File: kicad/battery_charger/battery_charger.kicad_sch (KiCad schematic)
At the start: 19 parts, among them J1 Conn_01x03_Pin, J2 USB_B_Micro, Q1 Q_PMOS_DSG, U1 TPS61200DRC, U2 MCP73831-2-OT

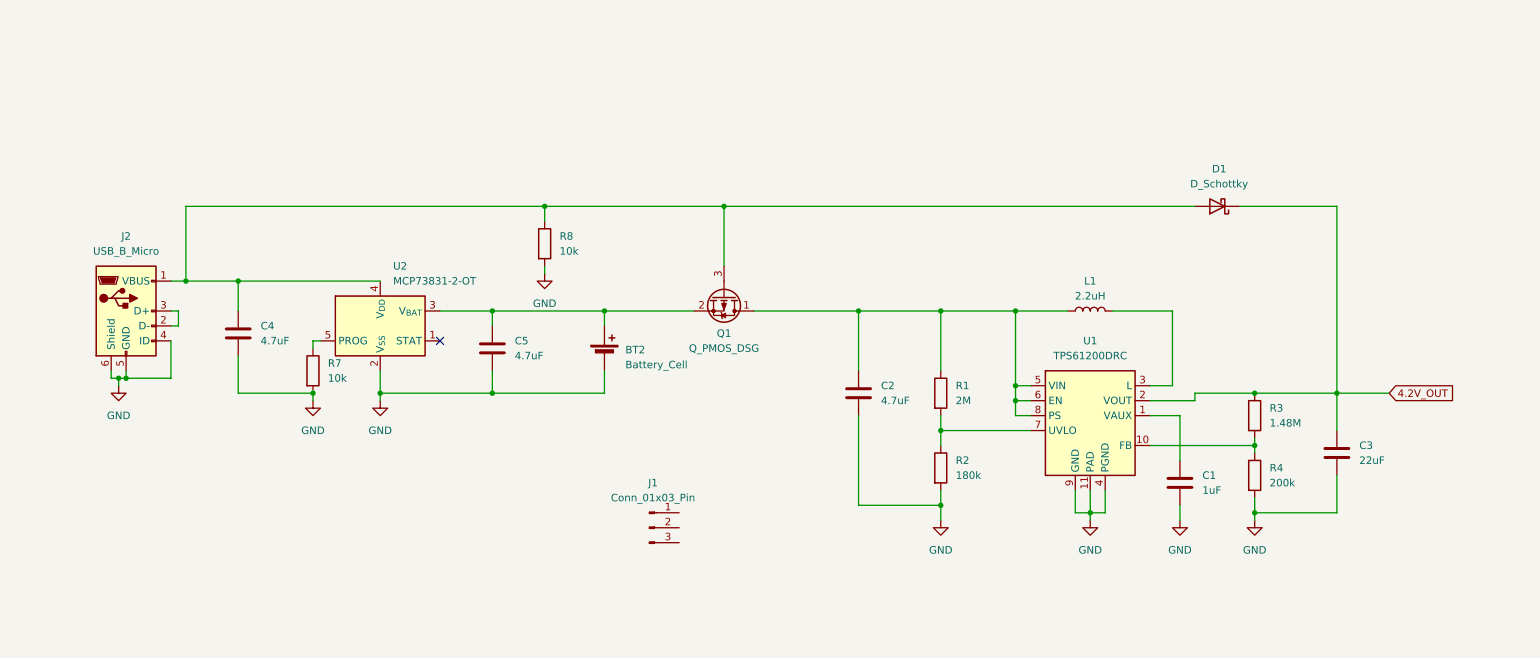
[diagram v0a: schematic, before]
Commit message: USB C compatible, added battery level indicator button
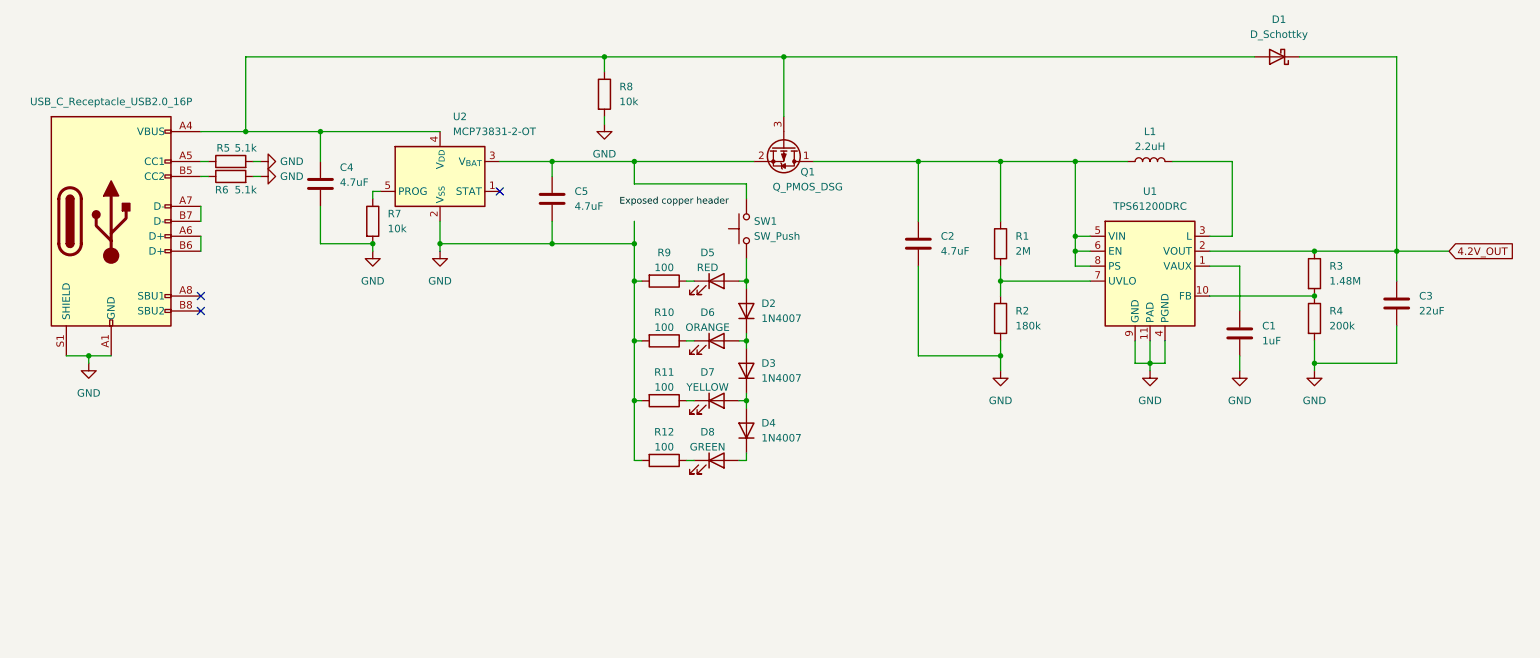
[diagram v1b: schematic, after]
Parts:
- removed BT2: Battery_Cell, symbol Device:Battery_Cell
- removed J1: Conn_01x03_Pin, symbol Connector:Conn_01x03_Pin
- removed J2: USB_B_Micro, symbol Connector:USB_B_Micro
- added D2, D3, D4: 1N4007, Diode_THT:D_DO-41_SOD81_P10.16mm_Horizontal, symbol Diode:1N4007
- added D5: RED, symbol Device:LED
- added D6: ORANGE, symbol Device:LED
- added D7: YELLOW, symbol Device:LED
- added D8: GREEN, symbol Device:LED
- added J1: USB_C_Receptacle_USB2.0_16P, symbol Connector:USB_C_Receptacle_USB2.0_16P
- added R10, R11, R12, R9: 100, symbol Device:R
- added R5, R6: 5.1k, symbol Device:R
- added SW1: SW_Push, symbol Switch:SW_Push
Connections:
- net GND: now also J1.A1 (GND), J1.A12 (GND), J1.B1 (GND), J1.B12 (GND), J1.S1 (SHIELD), R10.2, R11.2, R12.2, R5.2, R6.2, R9.2
- net at C5.1, Q1.2 (S), U2.3 (V_{BAT}): now also SW1.2
- net at C4.1, D1.2 (A), Q1.3 (G)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: now also J1.A4 (VBUS), J1.A9 (VBUS), J1.B4 (VBUS), J1.B9 (VBUS)
- new net: D5.1 (K), R9.1
- new net: D2.2 (A), D5.2 (A), SW1.1
- new net: D2.1 (K), D3.2 (A), D6.2 (A)
- new net: D4.1 (K), D8.2 (A)
- new net: D3.1 (K), D4.2 (A), D7.2 (A)
- new net: D8.1 (K), R12.1
- new net: J1.A5 (CC1), R5.1
- new net: J1.A6 (D+), J1.B6 (D+)
- new net: J1.A7 (D-), J1.B7 (D-)
- new net: J1.B5 (CC2), R6.1
- new net: D7.1 (K), R11.1
- new net: D6.1 (K), R10.1
- no-connect marks 1 -> 3
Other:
- title: (none) -> USB C Battery Charger and Source
- moved on the sheet: C1, C2, C3, C4, C5, D1, L1, Q1, R1, R2, R3, R4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

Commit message: made the pcb
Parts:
- C1: footprint (none) -> Capacitor_SMD:C_0402_1005Metric
- C2, C4, C5: footprint (none) -> Capacitor_SMD:C_0603_1608Metric
- C3: footprint (none) -> Capacitor_SMD:C_0805_2012Metric
- D1: footprint (none) -> Diode_SMD:D_0603_1608Metric
- D5, D6, D7, D8: footprint (none) -> LED_SMD:LED_0201_0603Metric
- J1: footprint (none) -> Connector_USB:USB_C_Receptacle_Amphenol_12401548E4-2A
- L1: footprint (none) -> Inductor_SMD:L_0603_1608Metric
- Q1: footprint (none) -> Package_DirectFET:DirectFET_MX
- R1, R10, R11, R12, R2, R3, R4, R5, R6, R7, R8, R9: footprint (none) -> Resistor_SMD:R_0603_1608Metric
- SW1: footprint (none) -> Button_Switch_THT:SW_PUSH_6mm
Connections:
- net at J1.A6 (D+): no longer J1.B6 (D+)
- net at J1.A7 (D-): no longer J1.B7 (D-)
- no-connect marks 3 -> 7
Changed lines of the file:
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@@
 	)
 	(no_connect
+		(at 52.07 62.23)
+	)
+	(no_connect
+		(at 52.07 69.85)
+	)
+	(no_connect
 		(at 52.07 77.47)
 	)
@@
 	)
 	(no_connect
+		(at 52.07 67.31)
+	)
+	(no_connect
+		(at 52.07 64.77)
+	)
+	(no_connect
 		(at 102.87 59.69)
 	)
@@
 	(wire
 		(pts
-			(xy 52.07 67.31) (xy 52.07 69.85)
-		)
-		(stroke
-			(width 0)
-			(type default)
-		)
-	)
-	(wire
-		(pts
 			(xy 241.3 69.85) (xy 255.27 69.85)
 		)
@@
 	(wire
 		(pts
-			(xy 52.07 62.23) (xy 52.07 64.77)
-		)
-		(stroke
-			(width 0)
-			(type default)
-		)
-	)
-	(wire
-		(pts
 			(xy 92.71 64.77) (xy 92.71 68.58)
 		)
@@
 			)
 		)
-		(property "Footprint" ""
+		(property "Footprint" "Package_DirectFET:DirectFET_MX"
 			(at 153.67 57.15 0)
 			(effects
@@
 			)
 		)
-		(property "Footprint" ""
+		(property "Footprint" "Resistor_SMD:R_0603_1608Metric"
 			(at 130.81 73.152 90)
 			(effects
@@
 			)
 		)
-		(property "Footprint" ""
+		(property "Footprint" "Button_Switch_THT:SW_PUSH_6mm"
 			(at 139.7 66.04 0)
 			(effects
@@
 			)
 		)
-		(property "Footprint" ""
+		(property "Footprint" "Resistor_SMD:R_0603_1608Metric"
 			(at 79.502 64.77 90)
 			(effects
@@
 			)
 		)
-		(property "Footprint" ""
+		(property "Footprint" "Resistor_SMD:R_0603_1608Metric"
 			(at 130.81 103.632 90)
 			(effects
@@
 			)
 		)
-		(property "Footprint" ""
+		(property "Footprint" "Capacitor_SMD:C_0402_1005Metric"
 			(at 229.5652 87.63 0)
 			(effects
@@
 			)
 		)
-		(property "Footprint" ""
+		(property "Footprint" "Connector_USB:USB_C_Receptacle_Amphenol_12401548E4-2A"
 			(at 40.64 64.77 0)
 			(effects
@@
 			)
 		)
-		(property "Footprint" ""
+		(property "Footprint" "Capacitor_SMD:C_0603_1608Metric"
 			(at 73.3552 62.23 0)
 			(effects
@@
 			)
 		)
-		(property "Footprint" ""
+		(property "Footprint" "Resistor_SMD:R_0603_1608Metric"
 			(at 130.81 93.472 90)
 			(effects
@@
 			)
 		)
-		(property "Footprint" ""
+		(property "Footprint" "Resistor_SMD:R_0603_1608Metric"
 			(at 239.522 73.66 90)
 			(effects
@@
 			)
 		)
-		(property "Footprint" ""
+		(property "Footprint" "Resistor_SMD:R_0603_1608Metric"
 			(at 57.15 58.928 90)
 			(effects
@@
 			)
 		)
-		(property "Footprint" ""
+		(property "Footprint" "Resistor_SMD:R_0603_1608Metric"
 			(at 57.15 56.388 90)
 			(effects
@@
 			)
 		)
-		(property "Footprint" ""
+		(property "Footprint" "LED_SMD:LED_0201_0603Metric"
 			(at 139.7 95.25 0)
 			(effects
@@
 			)
 		)
-		(property "Footprint" ""
+		(property "Footprint" "LED_SMD:LED_0201_0603Metric"
 			(at 139.7 74.93 0)
 			(effects
@@
 			)
 		)
-		(property "Footprint" ""
+		(property "Footprint" "LED_SMD:LED_0201_0603Metric"
 			(at 139.7 105.41 0)
 			(effects
@@
 			)
 		)
-		(property "Footprint" ""
+		(property "Footprint" "Diode_SMD:D_0603_1608Metric"
 			(at 234.95 36.83 0)
 			(effects
@@
 			)
 		)
-		(property "Footprint" ""
+		(property "Footprint" "Inductor_SMD:L_0603_1608Metric"
 			(at 213.36 54.61 0)
 			(effects
@@
 			)
 		)
-		(property "Footprint" ""
+		(property "Footprint" "LED_SMD:LED_0201_0603Metric"
 			(at 139.7 85.09 0)
 			(effects
@@
 			)
 		)
-		(property "Footprint" ""
+		(property "Footprint" "Resistor_SMD:R_0603_1608Metric"
 			(at 186.182 81.28 90)
 			(effects
@@
 			)
 		)
-		(property "Footprint" ""
+		(property "Footprint" "Resistor_SMD:R_0603_1608Metric"
 			(at 130.81 83.312 90)
 			(effects
@@
 			)
 		)
-		(property "Footprint" ""
+		(property "Footprint" "Resistor_SMD:R_0603_1608Metric"
 			(at 118.872 43.18 90)
 			(effects
@@
 			)
 		)
-		(property "Footprint" ""
+		(property "Footprint" "Capacitor_SMD:C_0603_1608Metric"
 			(at 174.9552 72.39 0)
 			(effects
@@
 			)
 		)
-		(property "Footprint" ""
+		(property "Footprint" "Resistor_SMD:R_0603_1608Metric"
 			(at 186.182 68.58 90)
 			(effects
@@
 			)
 		)
-		(property "Footprint" ""
+		(property "Footprint" "Capacitor_SMD:C_0805_2012Metric"
 			(at 256.2352 82.55 0)
 			(effects
@@
 			)
 		)
-		(property "Footprint" ""
+		(property "Footprint" "Resistor_SMD:R_0603_1608Metric"
 			(at 239.522 81.28 90)
 			(effects
@@
 			)
 		)
-		(property "Footprint" ""
+		(property "Footprint" "Capacitor_SMD:C_0603_1608Metric"
 			(at 112.7252 64.77 0)
 			(effects

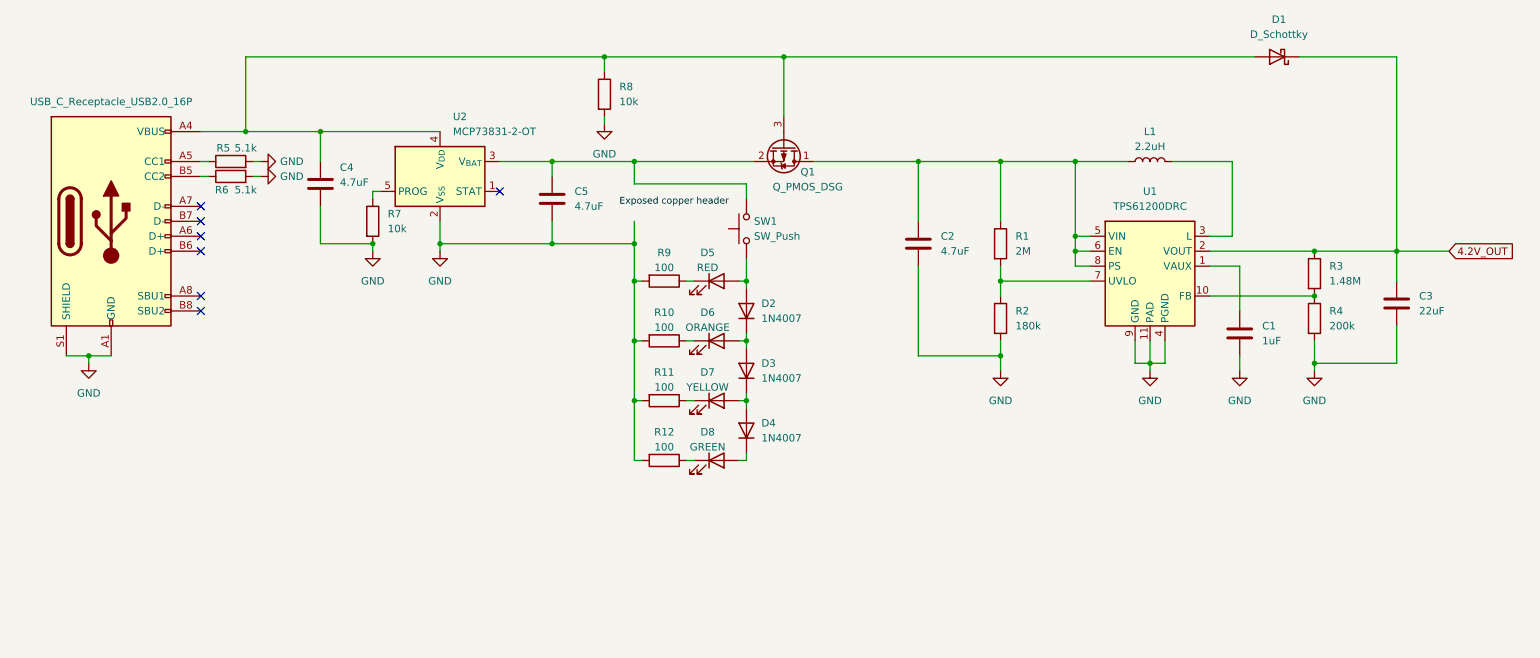
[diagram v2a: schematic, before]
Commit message: changed to usb b micro, made design longer and thinner
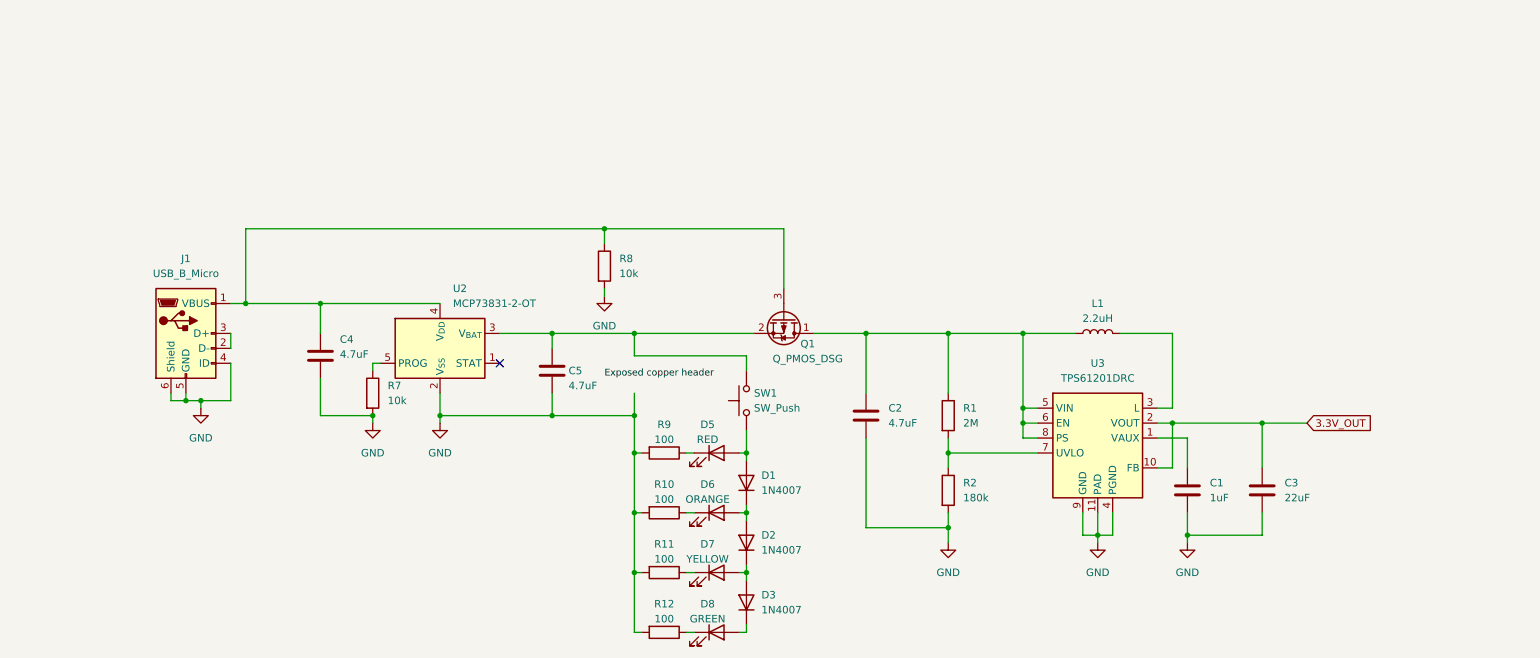
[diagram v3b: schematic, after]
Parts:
- removed D1: D_Schottky, Diode_SMD:D_0603_1608Metric, symbol Device:D_Schottky
- removed D4: 1N4007, Diode_THT:D_DO-41_SOD81_P10.16mm_Horizontal, symbol Diode:1N4007
- removed J1: USB_C_Receptacle_USB2.0_16P, Connector_USB:USB_C_Receptacle_Amphenol_12401548E4-2A, symbol Connector:USB_C_Receptacle_USB2.0_16P
- removed R3: 1.48M, Resistor_SMD:R_0603_1608Metric, symbol Device:R
- removed R4: 200k, Resistor_SMD:R_0603_1608Metric, symbol Device:R
- removed R5, R6: 5.1k, Resistor_SMD:R_0603_1608Metric, symbol Device:R
- removed U1: TPS61200DRC, Package_SON:Texas_S-PVSON-N10_ThermalVias, symbol Regulator_Switching:TPS61200DRC
- added D1: 1N4007, Library:SODFL3818X130N, symbol Diode:1N4007
- added J1: USB_B_Micro, Connector_USB:USB_Micro-B_Amphenol_10118193-0001LF_Horizontal, symbol Connector:USB_B_Micro
- added U3: TPS61201DRC, Library:TPS61201DRC, symbol Regulator_Switching:TPS61201DRC
- D2, D3: footprint Diode_THT:D_DO-41_SOD81_P10.16mm_Horizontal -> Library:SODFL3818X130N
- SW1: footprint Button_Switch_THT:SW_PUSH_6mm -> Button_Switch_SMD:SW_Push_1P1T-MP_NO_Horizontal_Alps_SKRTLAE010
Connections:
- net GND: now also J1.4 (ID), J1.5 (GND), J1.6 (Shield), U3.11 (PAD), U3.4 (PGND), U3.9 (GND)
- net at C2.1, L1.1, Q1.1 (D)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: now also U3.5 (VIN), U3.6 (EN), U3.8 (PS)
- net at C4.1, Q1.3 (G), R8.1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: now also J1.1 (VBUS)
- net at D5.2 (A), SW1.1: now also D1.2 (A); no longer D2.2 (A)
- net at D2.1 (K), D3.2 (A): now also D7.2 (A); no longer D6.2 (A)
- net at D8.2 (A): now also D3.1 (K)
- net at C1.1: now also U3.1 (VAUX)
- net at L1.2: now also U3.3 (L)
- net at R1.2, R2.1: now also U3.7 (UVLO)
- net 4.2V_OUT renamed 3.3V_OUT
- net 3.3V_OUT: now also U3.10 (FB), U3.2 (VOUT)
- new net: D1.1 (K), D2.2 (A), D6.2 (A)
- new net: J1.2 (D-), J1.3 (D+)
- no-connect marks 7 -> 1
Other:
- moved on the sheet: C1, C2, C3, C4, C5, D5, D6, D7, D8, L1, Q1, R1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

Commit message: neues aus dem labor
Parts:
- removed Q1: Q_PMOS_DSG, Package_DirectFET:DirectFET_MX, symbol Device:Q_PMOS_DSG
- added Q1: Q_PMOS_GSD, Package_TO_SOT_SMD:SOT-23-3, symbol Device:Q_PMOS_GSD
- D1, D2, D3: footprint Library:SODFL3818X130N -> Diode_SMD:D_SOD-123F
- D5, D6, D7, D8: footprint LED_SMD:LED_0201_0603Metric -> LED_SMD:LED_0402_1005Metric
- SW1: footprint Button_Switch_SMD:SW_Push_1P1T-MP_NO_Horizontal_Alps_SKRTLAE010 -> Button_Switch_SMD:SW_SPST_B3U-1000P
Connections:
- net at C2.1, L1.1, R1.1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: now also Q1.3 (D)
- net at C5.1, SW1.2, U2.3 (V_{BAT}): now also Q1.2 (S)
- net at C4.1, J1.1 (VBUS), R8.1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: now also Q1.1 (G)
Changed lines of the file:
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@@
-	)
-	(symbol
-		(lib_id "Device:Q_PMOS_DSG")
-		(at 151.13 81.28 270)
-		(unit 1)
-		(exclude_from_sim no)
-		(in_bom yes)
-		(on_board yes)
-		(dnp no)
-		(property "Reference" "Q1"
-			(at 155.194 85.598 90)
-			(effects
-				(font
-					(size 1.27 1.27)
-				)
-			)
-		)
-		(property "Value" "Q_PMOS_DSG"
-			(at 155.194 88.138 90)
-			(effects
-				(font
-					(size 1.27 1.27)
-				)
-			)
-		)
-		(property "Footprint" "Package_DirectFET:DirectFET_MX"
-			(at 153.67 86.36 0)
-			(effects
-				(font
-					(size 1.27 1.27)
-				)
-				(hide yes)
-			)
-		)
-		(property "Datasheet" "~"
-			(at 151.13 81.28 0)
-			(effects
-				(font
-					(size 1.27 1.27)
-				)
-				(hide yes)
-			)
-		)
-		(property "Description" "P-MOSFET transistor, drain/source/gate"
-			(at 151.13 81.28 0)
-			(effects
-				(font
-					(size 1.27 1.27)
-				)
-				(hide yes)
-			)
-		)
-		(pin "2"
-		)
-		(pin "1"
-		)
-		(pin "3"
-		)
-		(instances
-			(project ""
-				(path "/add37744-b832-4f24-98d5-20347e778715"
-					(reference "Q1")
-					(unit 1)
-				)
-			)
-		)
 	)
 	(symbol
@@
 			)
 		)
-		(property "Footprint" "Button_Switch_SMD:SW_Push_1P1T-MP_NO_Horizontal_Alps_SKRTLAE010"
+		(property "Footprint" "Button_Switch_SMD:SW_SPST_B3U-1000P"
 			(at 139.7 95.25 0)
 			(effects
@@
 	)
 	(symbol
+		(lib_id "Device:Q_PMOS_GSD")
+		(at 151.13 81.28 270)
+		(unit 1)
+		(exclude_from_sim no)
+		(in_bom yes)
+		(on_board yes)
+		(dnp no)
+		(property "Reference" "Q1"
+			(at 151.13 87.63 90)
+			(effects
+				(font
+					(size 1.27 1.27)
+				)
+			)
+		)
+		(property "Value" "Q_PMOS_GSD"
+			(at 156.718 90.17 90)
+			(effects
+				(font
+					(size 1.27 1.27)
+				)
+			)
+		)
+		(property "Footprint" "Package_TO_SOT_SMD:SOT-23-3"
+			(at 153.67 86.36 0)
+			(effects
+				(font
+					(size 1.27 1.27)
+				)
+				(hide yes)
+			)
+		)
+		(property "Datasheet" "~"
+			(at 151.13 81.28 0)
+			(effects
+				(font
+					(size 1.27 1.27)
+				)
+				(hide yes)
+			)
+		)
+		(property "Description" "P-MOSFET transistor, gate/source/drain"
+			(at 151.13 81.28 0)
+			(effects
+				(font
+					(size 1.27 1.27)
+				)
+				(hide yes)
+			)
+		)
+		(pin "3"
+		)
+		(pin "2"
+		)
+		(pin "1"
+		)
+		(instances
+			(project ""
+				(path "/add37744-b832-4f24-98d5-20347e778715"
+					(reference "Q1")
+					(unit 1)
+				)
+			)
+		)
+	)
+	(symbol
 		(lib_id "power:GND")
 		(at 204.47 119.38 0)
@@
 			)
 		)
-		(property "Footprint" "LED_SMD:LED_0201_0603Metric"
+		(property "Footprint" "LED_SMD:LED_0402_1005Metric"
 			(at 139.7 124.46 0)
 			(effects
@@
 			)
 		)
-		(property "Footprint" "LED_SMD:LED_0201_0603Metric"
+		(property "Footprint" "LED_SMD:LED_0402_1005Metric"
 			(at 139.7 104.14 0)
 			(effects
@@
 			)
 		)
-		(property "Footprint" "LED_SMD:LED_0201_0603Metric"
+		(property "Footprint" "LED_SMD:LED_0402_1005Metric"
 			(at 139.7 134.62 0)
 			(effects
@@
 			)
 		)
-		(property "Footprint" "LED_SMD:LED_0201_0603Metric"
+		(property "Footprint" "LED_SMD:LED_0402_1005Metric"
 			(at 139.7 114.3 0)
 			(effects
@@
 			)
 		)
-		(property "Footprint" "Library:SODFL3818X130N"
+		(property "Footprint" "Diode_SMD:D_SOD-123F"
 			(at 149.225 129.54 0)
 			(effects
@@
 			)
 		)
-		(property "Footprint" "Library:SODFL3818X130N"
+		(property "Footprint" "Diode_SMD:D_SOD-123F"
 			(at 149.225 109.22 0)
 			(effects
@@
 			)
 		)
-		(property "Footprint" "Library:SODFL3818X130N"
+		(property "Footprint" "Diode_SMD:D_SOD-123F"
 			(at 149.225 119.38 0)
 			(effects
